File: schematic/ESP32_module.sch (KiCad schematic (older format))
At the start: 14 parts, among them J1 Conn_02x03_Odd_Even, J2 Conn_02x05_Odd_Even, J3 Conn_02x06_Odd_Even, U1 ESP32-WROOM-32

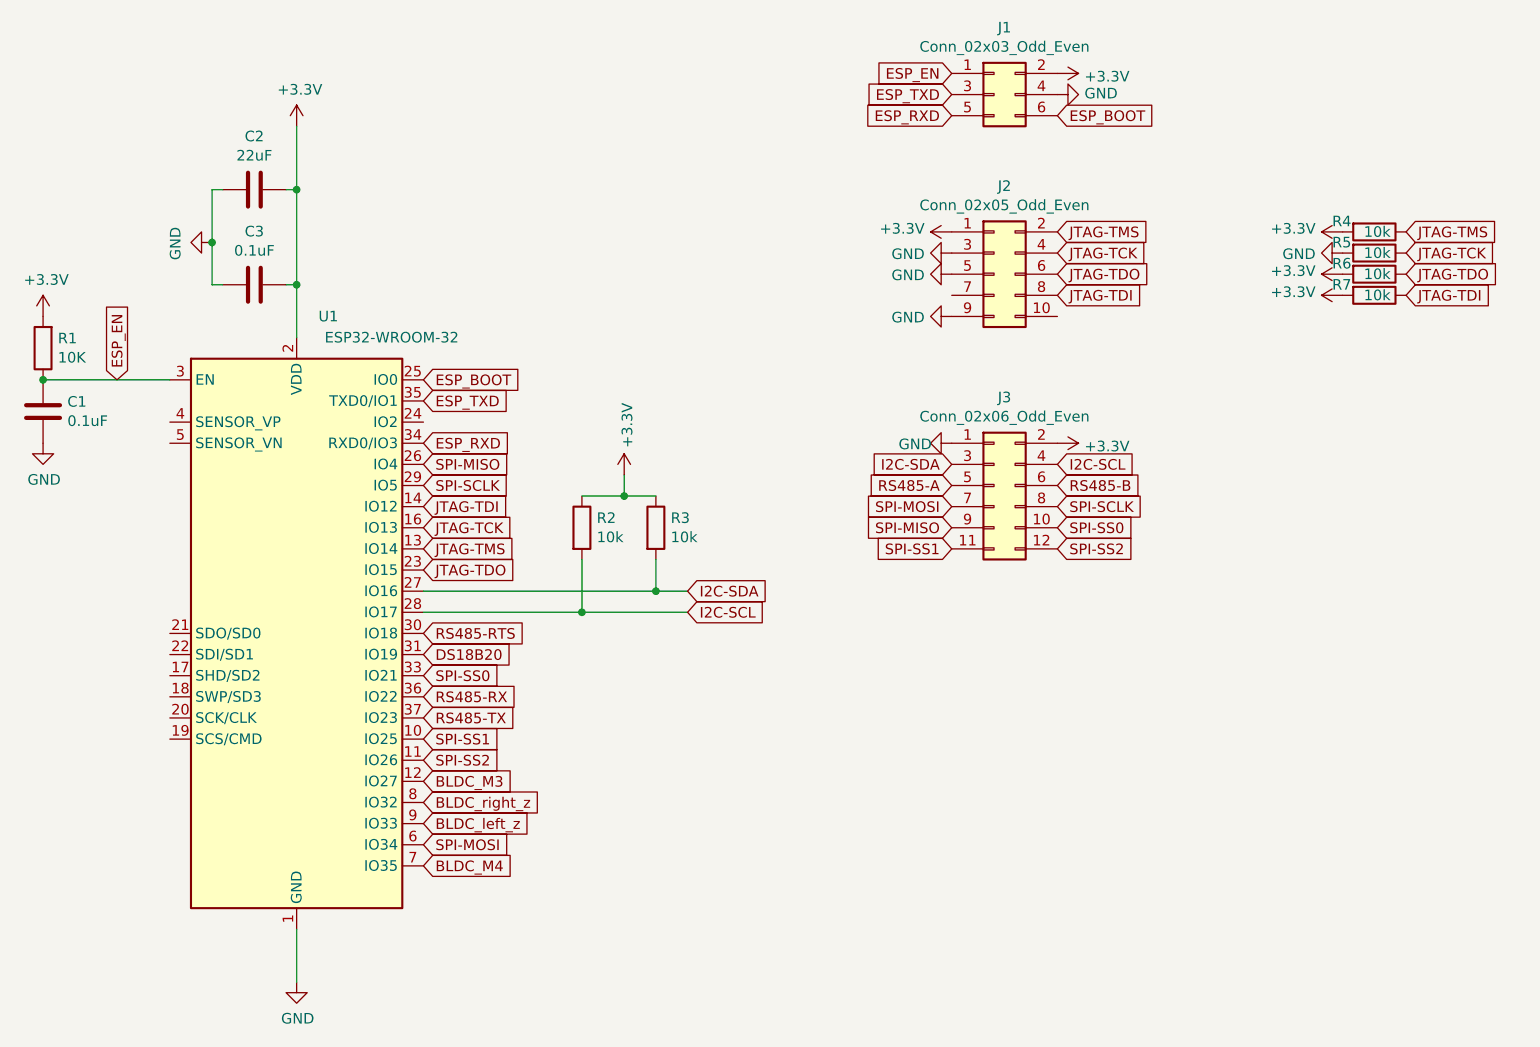
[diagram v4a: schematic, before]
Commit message: added MAX6682 for termistor
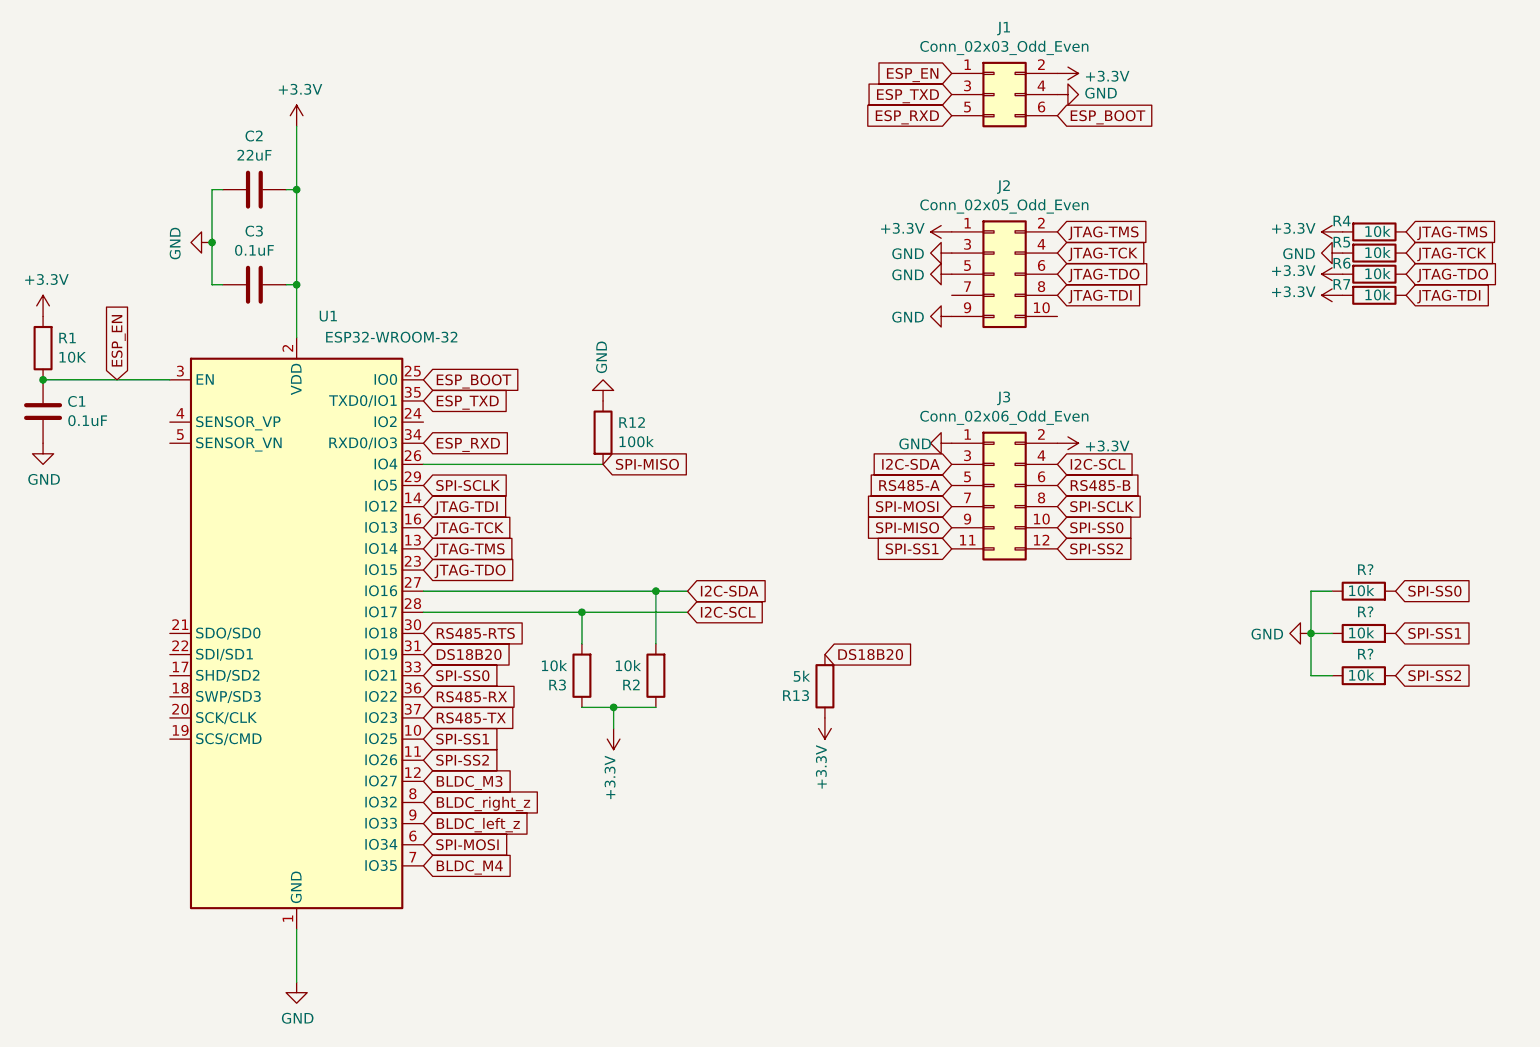
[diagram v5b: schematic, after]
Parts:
- added R12: 100k, symbol Device:R
- added R13: 5k, Resistor_SMD:R_0805_2012Metric_Pad1.15x1.40mm_HandSolder, symbol Device:R
- added R? (x3): 10k, Resistor_SMD:R_0805_2012Metric_Pad1.15x1.40mm_HandSolder, symbol Device:R
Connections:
- net +3V3: now also R13.1
- net DS18B20: now also R13.2
- net GND: now also R12.1, R?.1, R?.1, R?.1
- net I2C-SCL: now also R3.2; no longer R2.2
- net I2C-SDA: now also R2.2; no longer R3.2
- net SPI-MISO: now also R12.2
- net SPI-SS0: now also R?.2
- net SPI-SS1: now also R?.2
- net SPI-SS2: now also R?.2
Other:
- moved on the sheet: R2, R3
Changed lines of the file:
@@
 L Device:R R2
 U 1 1 5EE7A7CF
-P 3900 3800
-F 0 "R2" H 3970 3846 50  0000 L CNN
-F 1 "10k" H 3970 3755 50  0000 L CNN
-F 2 "Resistor_SMD:R_0805_2012Metric_Pad1.15x1.40mm_HandSolder" V 3830 3800 50  0001 C CNN
-F 3 "~" H 3900 3800 50  0001 C CNN
-	1    3900 3800
-	1    0    0    -1
+P 4250 4500
+F 0 "R2" H 4320 4546 50  0000 L CNN
+F 1 "10k" H 4320 4455 50  0000 L CNN
+F 2 "Resistor_SMD:R_0805_2012Metric_Pad1.15x1.40mm_HandSolder" V 4180 4500 50  0001 C CNN
+F 3 "~" H 4250 4500 50  0001 C CNN
+	1    4250 4500
+	-1   0    0    1
 $EndComp
 $Comp
 L Device:R R3
 U 1 1 5EE7A7D6
-P 4250 3800
-F 0 "R3" H 4320 3846 50  0000 L CNN
-F 1 "10k" H 4320 3755 50  0000 L CNN
-F 2 "Resistor_SMD:R_0805_2012Metric_Pad1.15x1.40mm_HandSolder" V 4180 3800 50  0001 C CNN
-F 3 "~" H 4250 3800 50  0001 C CNN
-	1    4250 3800
-	1    0    0    -1
+P 3900 4500
+F 0 "R3" H 3970 4546 50  0000 L CNN
+F 1 "10k" H 3970 4455 50  0000 L CNN
+F 2 "Resistor_SMD:R_0805_2012Metric_Pad1.15x1.40mm_HandSolder" V 3830 4500 50  0001 C CNN
+F 3 "~" H 3900 4500 50  0001 C CNN
+	1    3900 4500
+	-1   0    0    1
 $EndComp
 Text GLabel 3150 5300 2    50   Input ~ 0
 SPI-MOSI
-Text GLabel 3150 3500 2    50   Input ~ 0
+Text GLabel 4000 3500 2    50   Input ~ 0
 SPI-MISO
 Text GLabel 3150 3600 2    50   Input ~ 0
@@
 L power:+3.3V #PWR?
 U 1 1 5EE96C0B
-P 4100 3550
+P 4050 4750
 AR Path="/5EE96C0B" Ref="#PWR?"  Part="1"
 AR Path="/5ED629AF/5EE96C0B" Ref="#PWR06"  Part="1"
-F 0 "#PWR06" H 4100 3400 50  0001 C CNN
-F 1 "+3.3V" V 4115 3678 50  0000 L CNN
-F 2 "" H 4100 3550 50  0001 C CNN
-F 3 "" H 4100 3550 50  0001 C CNN
-	1    4100 3550
-	1    0    0    -1
+F 0 "#PWR06" H 4050 4600 50  0001 C CNN
+F 1 "+3.3V" V 4065 4878 50  0000 L CNN
+F 2 "" H 4050 4750 50  0001 C CNN
+F 3 "" H 4050 4750 50  0001 C CNN
+	1    4050 4750
+	-1   0    0    1
 $EndComp
 $Comp
@@
 Text GLabel 5650 3700 0    50   Input ~ 0
 SPI-MOSI
-Text GLabel 5650 3800 0    50   Input ~ 0
-SPI-MISO
 Text GLabel 6150 3700 2    50   Input ~ 0
 SPI-SCLK
@@
 	3150 4200 3900 4200
 Wire Wire Line
-	3900 3950 3900 4200
+	4250 4350 4250 4100
 Connection ~ 3900 4200
 Wire Wire Line
 	3900 4200 4400 4200
 Wire Wire Line
-	4250 3950 4250 4100
+	3900 4350 3900 4200
 Connection ~ 4250 4100
 Wire Wire Line
 	4250 4100 4400 4100
 Wire Wire Line
-	3900 3650 4100 3650
-Wire Wire Line
-	4100 3550 4100 3650
-Connection ~ 4100 3650
-Wire Wire Line
-	4100 3650 4250 3650
+	4250 4650 4050 4650
+Wire Wire Line
+	4050 4750 4050 4650
+Connection ~ 4050 4650
+Wire Wire Line
+	4050 4650 3900 4650
 Text GLabel 6150 2700 2    50   Input ~ 0
 JTAG-TDI
@@
 Text GLabel 3150 4900 2    50   Input ~ 0
 SPI-SS2
+$Comp
+L Device:R R12
+U 1 1 5EF62F89
+P 4000 3350
+F 0 "R12" H 4070 3396 50  0000 L CNN
+F 1 "100k" H 4070 3305 50  0000 L CNN
+F 2 "" V 3930 3350 50  0001 C CNN
+F 3 "~" H 4000 3350 50  0001 C CNN
+	1    4000 3350
+	1    0    0    -1
+$EndComp
+Wire Wire Line
+	4000 3500 3150 3500
+$Comp
+L power:GND #PWR?
+U 1 1 5EF653F3
+P 4000 3200
+AR Path="/5EF653F3" Ref="#PWR?"  Part="1"
+AR Path="/5ED629AF/5EF653F3" Ref="#PWR0101"  Part="1"
+F 0 "#PWR0101" H 4000 2950 50  0001 C CNN
+F 1 "GND" V 4005 3072 50  0000 R CNN
+F 2 "" H 4000 3200 50  0001 C CNN
+F 3 "" H 4000 3200 50  0001 C CNN
+	1    4000 3200
+	-1   0    0    1
+$EndComp
+Text GLabel 5050 4400 2    50   Input ~ 0
+DS18B20
+$Comp
+L Device:R R13
+U 1 1 5EF994A3
+P 5050 4550
+F 0 "R13" H 5120 4596 50  0000 L CNN
+F 1 "5k" H 5120 4505 50  0000 L CNN
+F 2 "Resistor_SMD:R_0805_2012Metric_Pad1.15x1.40mm_HandSolder" V 4980 4550 50  0001 C CNN
+F 3 "~" H 5050 4550 50  0001 C CNN
+	1    5050 4550
+	-1   0    0    1
+$EndComp
+$Comp
+L power:+3.3V #PWR?
+U 1 1 5EF99A29
+P 5050 4700
+AR Path="/5EF99A29" Ref="#PWR?"  Part="1"
+AR Path="/5ED629AF/5EF99A29" Ref="#PWR0102"  Part="1"
+F 0 "#PWR0102" H 5050 4550 50  0001 C CNN
+F 1 "+3.3V" V 5065 4828 50  0000 L CNN
+F 2 "" H 5050 4700 50  0001 C CNN
+F 3 "" H 5050 4700 50  0001 C CNN
+	1    5050 4700
+	-1   0    0    1
+$EndComp
+Text GLabel 5650 3800 0    50   Input ~ 0
+SPI-MISO
+Text GLabel 7750 4100 2    50   Input ~ 0
+SPI-SS0
+Text GLabel 7750 4500 2    50   Input ~ 0
+SPI-SS2
+Text GLabel 7750 4300 2    50   Input ~ 0
+SPI-SS1
+$Comp
+L Device:R R?
+U 1 1 5F10E23C
+P 7600 4500
+F 0 "R?" V 7700 4450 50  0000 L CNN
+F 1 "10k" V 7600 4450 50  0000 L CNN
+F 2 "Resistor_SMD:R_0805_2012Metric_Pad1.15x1.40mm_HandSolder" V 7530 4500 50  0001 C CNN
+F 3 "~" H 7600 4500 50  0001 C CNN
+	1    7600 4500
+	0    -1   -1   0
+$EndComp
+$Comp
+L Device:R R?
+U 1 1 5F10F25F
+P 7600 4300
+F 0 "R?" V 7700 4250 50  0000 L CNN
+F 1 "10k" V 7600 4250 50  0000 L CNN
+F 2 "Resistor_SMD:R_0805_2012Metric_Pad1.15x1.40mm_HandSolder" V 7530 4300 50  0001 C CNN
+F 3 "~" H 7600 4300 50  0001 C CNN
+	1    7600 4300
+	0    -1   -1   0
+$EndComp
+$Comp
+L Device:R R?
+U 1 1 5F10F5B3
+P 7600 4100
+F 0 "R?" V 7700 4050 50  0000 L CNN
+F 1 "10k" V 7600 4050 50  0000 L CNN
+F 2 "Resistor_SMD:R_0805_2012Metric_Pad1.15x1.40mm_HandSolder" V 7530 4100 50  0001 C CNN
+F 3 "~" H 7600 4100 50  0001 C CNN
+	1    7600 4100
+	0    -1   -1   0
+$EndComp
+$Comp
+L power:GND #PWR?
+U 1 1 5F1101D6
+P 7350 4300
+AR Path="/5F1101D6" Ref="#PWR?"  Part="1"
+AR Path="/5ED629AF/5F1101D6" Ref="#PWR?"  Part="1"
+F 0 "#PWR?" H 7350 4050 50  0001 C CNN
+F 1 "GND" V 7355 4172 50  0000 R CNN
+F 2 "" H 7350 4300 50  0001 C CNN
+F 3 "" H 7350 4300 50  0001 C CNN
+	1    7350 4300
+	0    1    1    0
+$EndComp
+Wire Wire Line
+	7450 4500 7350 4500
+Wire Wire Line
+	7350 4500 7350 4300
+Wire Wire Line
+	7350 4100 7450 4100
+Connection ~ 7350 4300
+Wire Wire Line
+	7350 4300 7350 4100
+Wire Wire Line
+	7450 4300 7350 4300
 $EndSCHEMATC

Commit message: new components on pcb
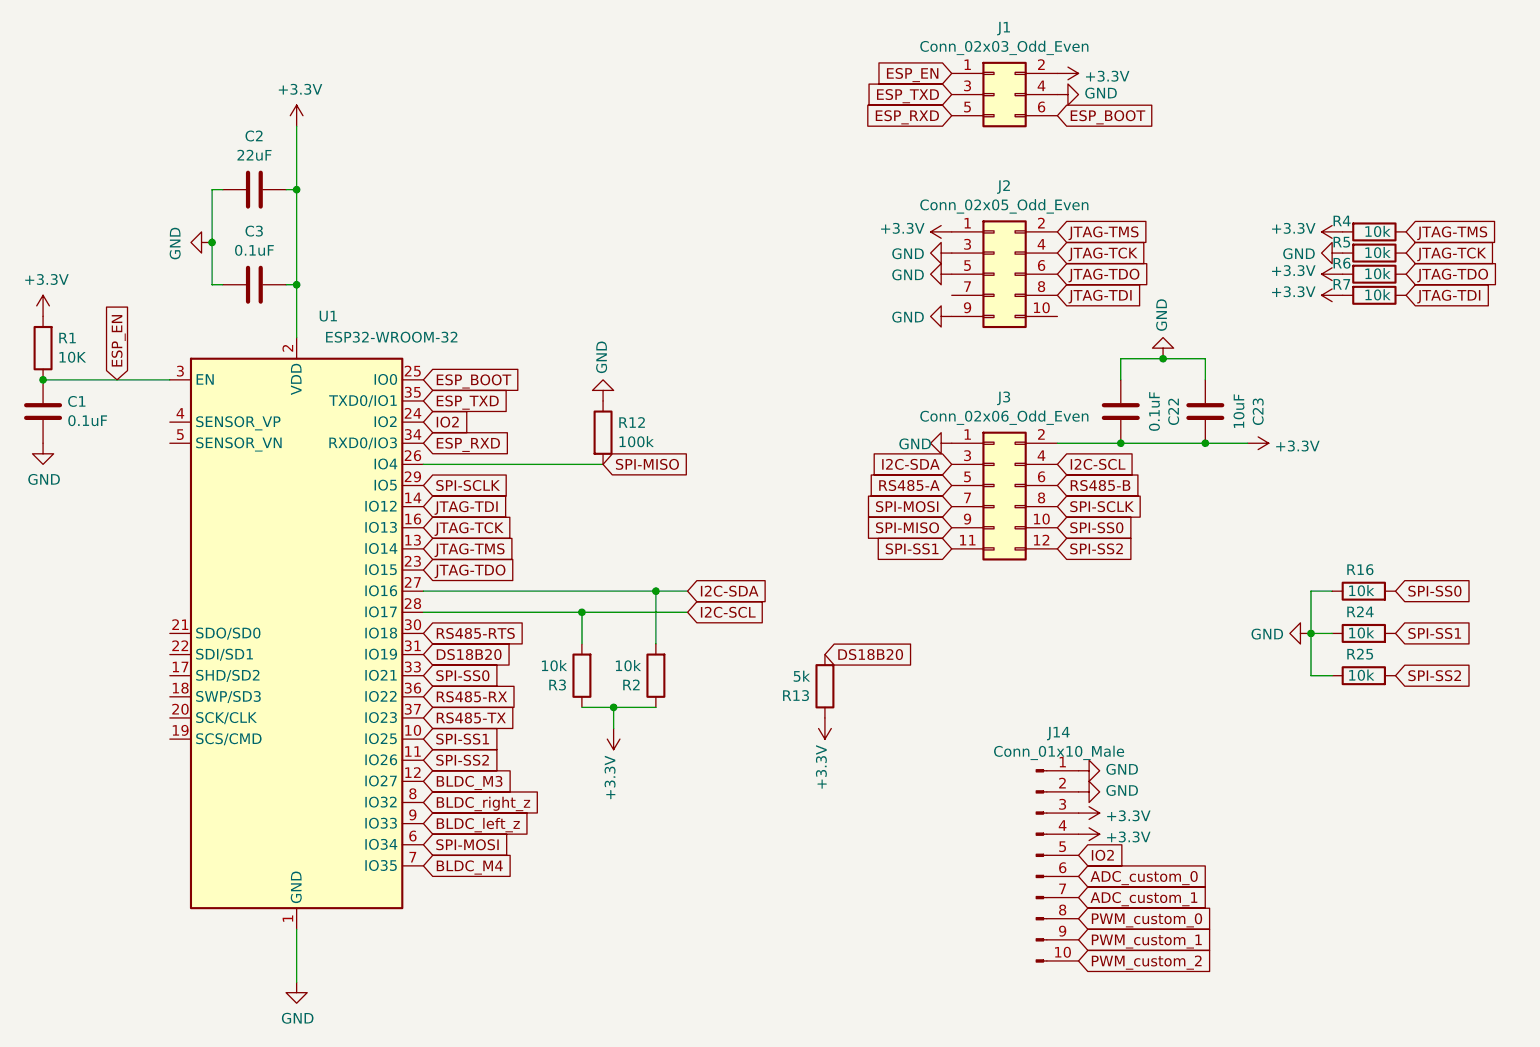
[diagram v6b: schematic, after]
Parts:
- added C22: 0.1uF, Capacitor_SMD:C_0805_2012Metric_Pad1.15x1.40mm_HandSolder, symbol Device:C
- added C23: 10uF, Capacitor_SMD:C_0805_2012Metric_Pad1.15x1.40mm_HandSolder, symbol Device:C
- added J14: Conn_01x10_Male, Connector_PinHeader_2.54mm:PinHeader_1x10_P2.54mm_Vertical, symbol Connector:Conn_01x10_Male
- R12: footprint (none) -> Resistor_SMD:R_0805_2012Metric_Pad1.15x1.40mm_HandSolder
- gave numbers to parts that had none: 3
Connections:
- net +3V3: now also C22.2, C23.2, J14.3 (Pin_3), J14.4 (Pin_4)
- net GND: now also C22.1, C23.1, J14.1 (Pin_1), J14.2 (Pin_2)
- net IO2: now reaches U1.24 (IO2)
- net IO2: now also J14.5 (Pin_5)
- new net ADC_custom_0: J14.6 (Pin_6)
- new net ADC_custom_1: J14.7 (Pin_7)
- new net PWM_custom_0: J14.8 (Pin_8)
- new net PWM_custom_1: J14.9 (Pin_9)
- new net PWM_custom_2: J14.10 (Pin_10)
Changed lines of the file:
@@
 L power:+3.3V #PWR?
 U 1 1 5EF14A29
-P 6150 3400
+P 7050 3400
 AR Path="/5EF14A29" Ref="#PWR?"  Part="1"
 AR Path="/5ED629AF/5EF14A29" Ref="#PWR014"  Part="1"
-F 0 "#PWR014" H 6150 3250 50  0001 C CNN
-F 1 "+3.3V" V 6165 3528 50  0000 L CNN
-F 2 "" H 6150 3400 50  0001 C CNN
-F 3 "" H 6150 3400 50  0001 C CNN
-	1    6150 3400
+F 0 "#PWR014" H 7050 3250 50  0001 C CNN
+F 1 "+3.3V" V 7065 3528 50  0000 L CNN
+F 2 "" H 7050 3400 50  0001 C CNN
+F 3 "" H 7050 3400 50  0001 C CNN
+	1    7050 3400
 	0    1    1    0
 $EndComp
@@
 F 0 "R12" H 4070 3396 50  0000 L CNN
 F 1 "100k" H 4070 3305 50  0000 L CNN
-F 2 "" V 3930 3350 50  0001 C CNN
+F 2 "Resistor_SMD:R_0805_2012Metric_Pad1.15x1.40mm_HandSolder" V 3930 3350 50  0001 C CNN
 F 3 "~" H 4000 3350 50  0001 C CNN
 	1    4000 3350
@@
 SPI-SS1
 $Comp
-L Device:R R?
+L Device:R R25
 U 1 1 5F10E23C
 P 7600 4500
-F 0 "R?" V 7700 4450 50  0000 L CNN
+F 0 "R25" V 7700 4450 50  0000 L CNN
 F 1 "10k" V 7600 4450 50  0000 L CNN
 F 2 "Resistor_SMD:R_0805_2012Metric_Pad1.15x1.40mm_HandSolder" V 7530 4500 50  0001 C CNN
@@
 $EndComp
 $Comp
-L Device:R R?
+L Device:R R24
 U 1 1 5F10F25F
 P 7600 4300
-F 0 "R?" V 7700 4250 50  0000 L CNN
+F 0 "R24" V 7700 4250 50  0000 L CNN
 F 1 "10k" V 7600 4250 50  0000 L CNN
 F 2 "Resistor_SMD:R_0805_2012Metric_Pad1.15x1.40mm_HandSolder" V 7530 4300 50  0001 C CNN
@@
 $EndComp
 $Comp
-L Device:R R?
+L Device:R R16
 U 1 1 5F10F5B3
 P 7600 4100
-F 0 "R?" V 7700 4050 50  0000 L CNN
+F 0 "R16" V 7700 4050 50  0000 L CNN
 F 1 "10k" V 7600 4050 50  0000 L CNN
 F 2 "Resistor_SMD:R_0805_2012Metric_Pad1.15x1.40mm_HandSolder" V 7530 4100 50  0001 C CNN
@@
 P 7350 4300
 AR Path="/5F1101D6" Ref="#PWR?"  Part="1"
-AR Path="/5ED629AF/5F1101D6" Ref="#PWR?"  Part="1"
-F 0 "#PWR?" H 7350 4050 50  0001 C CNN
+AR Path="/5ED629AF/5F1101D6" Ref="#PWR0103"  Part="1"
+F 0 "#PWR0103" H 7350 4050 50  0001 C CNN
 F 1 "GND" V 7355 4172 50  0000 R CNN
 F 2 "" H 7350 4300 50  0001 C CNN
@@
 Wire Wire Line
 	7450 4300 7350 4300
+$Comp
+L Connector:Conn_01x10_Male J14
+U 1 1 5EFA3108
+P 6050 5350
+F 0 "J14" H 6158 5931 50  0000 C CNN
+F 1 "Conn_01x10_Male" H 6158 5840 50  0000 C CNN
+F 2 "Connector_PinHeader_2.54mm:PinHeader_1x10_P2.54mm_Vertical" H 6050 5350 50  0001 C CNN
+F 3 "~" H 6050 5350 50  0001 C CNN
+	1    6050 5350
+	1    0    0    -1
+$EndComp
+Text GLabel 3150 3300 2    50   Input ~ 0
+IO2
+$Comp
+L power:GND #PWR?
+U 1 1 5EFA6B4A
+P 6250 4950
+AR Path="/5EFA6B4A" Ref="#PWR?"  Part="1"
+AR Path="/5ED629AF/5EFA6B4A" Ref="#PWR0109"  Part="1"
+F 0 "#PWR0109" H 6250 4700 50  0001 C CNN
+F 1 "GND" V 6255 4822 50  0000 R CNN
+F 2 "" H 6250 4950 50  0001 C CNN
+F 3 "" H 6250 4950 50  0001 C CNN
+	1    6250 4950
+	0    -1   -1   0
+$EndComp
+$Comp
+L power:+3.3V #PWR?
+U 1 1 5EFA72FF
+P 6250 5150
+AR Path="/5EFA72FF" Ref="#PWR?"  Part="1"
+AR Path="/5ED629AF/5EFA72FF" Ref="#PWR0110"  Part="1"
+F 0 "#PWR0110" H 6250 5000 50  0001 C CNN
+F 1 "+3.3V" V 6265 5278 50  0000 L CNN
+F 2 "" H 6250 5150 50  0001 C CNN
+F 3 "" H 6250 5150 50  0001 C CNN
+	1    6250 5150
+	0    1    1    0
+$EndComp
+Text GLabel 6250 5350 2    50   Input ~ 0
+IO2
+$Comp
+L power:+3.3V #PWR?
+U 1 1 5EFAB189
+P 6250 5250
+AR Path="/5EFAB189" Ref="#PWR?"  Part="1"
+AR Path="/5ED629AF/5EFAB189" Ref="#PWR0111"  Part="1"
+F 0 "#PWR0111" H 6250 5100 50  0001 C CNN
+F 1 "+3.3V" V 6265 5378 50  0000 L CNN
+F 2 "" H 6250 5250 50  0001 C CNN
+F 3 "" H 6250 5250 50  0001 C CNN
+	1    6250 5250
+	0    1    1    0
+$EndComp
+$Comp
+L power:GND #PWR?
+U 1 1 5EFAB62F
+P 6250 5050
+AR Path="/5EFAB62F" Ref="#PWR?"  Part="1"
+AR Path="/5ED629AF/5EFAB62F" Ref="#PWR0112"  Part="1"
+F 0 "#PWR0112" H 6250 4800 50  0001 C CNN
+F 1 "GND" V 6255 4922 50  0000 R CNN
+F 2 "" H 6250 5050 50  0001 C CNN
+F 3 "" H 6250 5050 50  0001 C CNN
+	1    6250 5050
+	0    -1   -1   0
+$EndComp
+Text GLabel 6250 5450 2    50   Input ~ 0
+ADC_custom_0
+Text GLabel 6250 5550 2    50   Input ~ 0
+ADC_custom_1
+Text GLabel 6250 5650 2    50   Input ~ 0
+PWM_custom_0
+Text GLabel 6250 5750 2    50   Input ~ 0
+PWM_custom_1
+Text GLabel 6250 5850 2    50   Input ~ 0
+PWM_custom_2
+$Comp
+L Device:C C22
+U 1 1 5EFE505D
+P 6450 3250
+F 0 "C22" V 6702 3250 50  0000 C CNN
+F 1 "0.1uF" V 6611 3250 50  0000 C CNN
+F 2 "Capacitor_SMD:C_0805_2012Metric_Pad1.15x1.40mm_HandSolder" H 6488 3100 50  0001 C CNN
+F 3 "~" H 6450 3250 50  0001 C CNN
+	1    6450 3250
+	1    0    0    -1
+$EndComp
+$Comp
+L Device:C C23
+U 1 1 5EFE96D8
+P 6850 3250
+F 0 "C23" V 7102 3250 50  0000 C CNN
+F 1 "10uF" V 7011 3250 50  0000 C CNN
+F 2 "Capacitor_SMD:C_0805_2012Metric_Pad1.15x1.40mm_HandSolder" H 6888 3100 50  0001 C CNN
+F 3 "~" H 6850 3250 50  0001 C CNN
+	1    6850 3250
+	1    0    0    -1
+$EndComp
+Wire Wire Line
+	6150 3400 6450 3400
+Connection ~ 6450 3400
+Wire Wire Line
+	6450 3400 6850 3400
+Connection ~ 6850 3400
+Wire Wire Line
+	6850 3400 7050 3400
+Wire Wire Line
+	6450 3100 6450 3000
+Wire Wire Line
+	6450 3000 6650 3000
+Wire Wire Line
+	6850 3000 6850 3100
+$Comp
+L power:GND #PWR?
+U 1 1 5EFEB145
+P 6650 3000
+AR Path="/5EFEB145" Ref="#PWR?"  Part="1"
+AR Path="/5ED629AF/5EFEB145" Ref="#PWR0115"  Part="1"
+F 0 "#PWR0115" H 6650 2750 50  0001 C CNN
+F 1 "GND" V 6655 2872 50  0000 R CNN
+F 2 "" H 6650 3000 50  0001 C CNN
+F 3 "" H 6650 3000 50  0001 C CNN
+	1    6650 3000
+	-1   0    0    1
+$EndComp
+Connection ~ 6650 3000
+Wire Wire Line
+	6650 3000 6850 3000
 $EndSCHEMATC
